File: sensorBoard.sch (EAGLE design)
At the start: 37 parts, among them U1 BME280, U2 nRF8001, U3 MIC5225-3.3v, U4 74HC4050D, Y1 16MHz, Y2 FC-255 32.7680K-A3

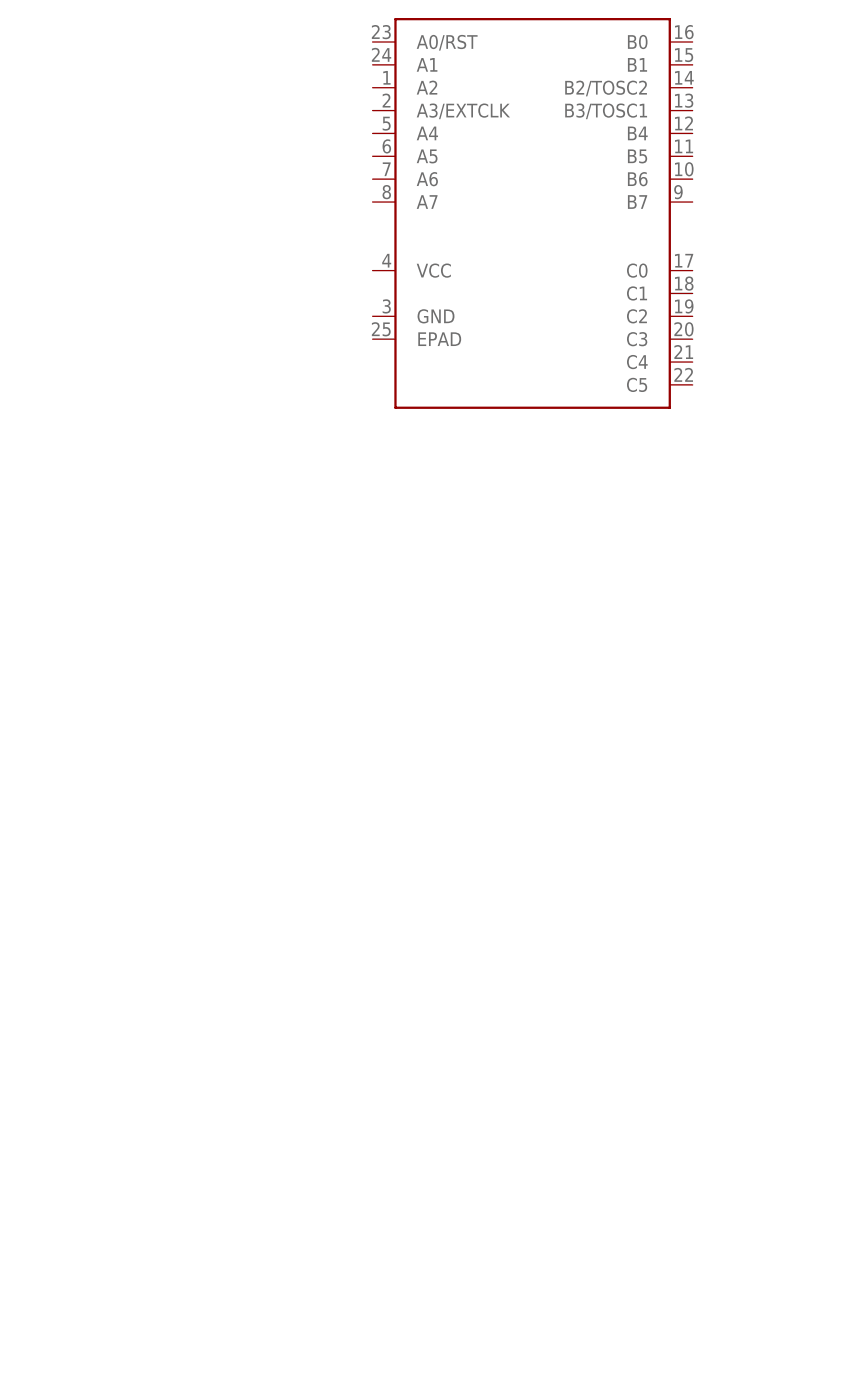
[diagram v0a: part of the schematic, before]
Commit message: Created proto PCB
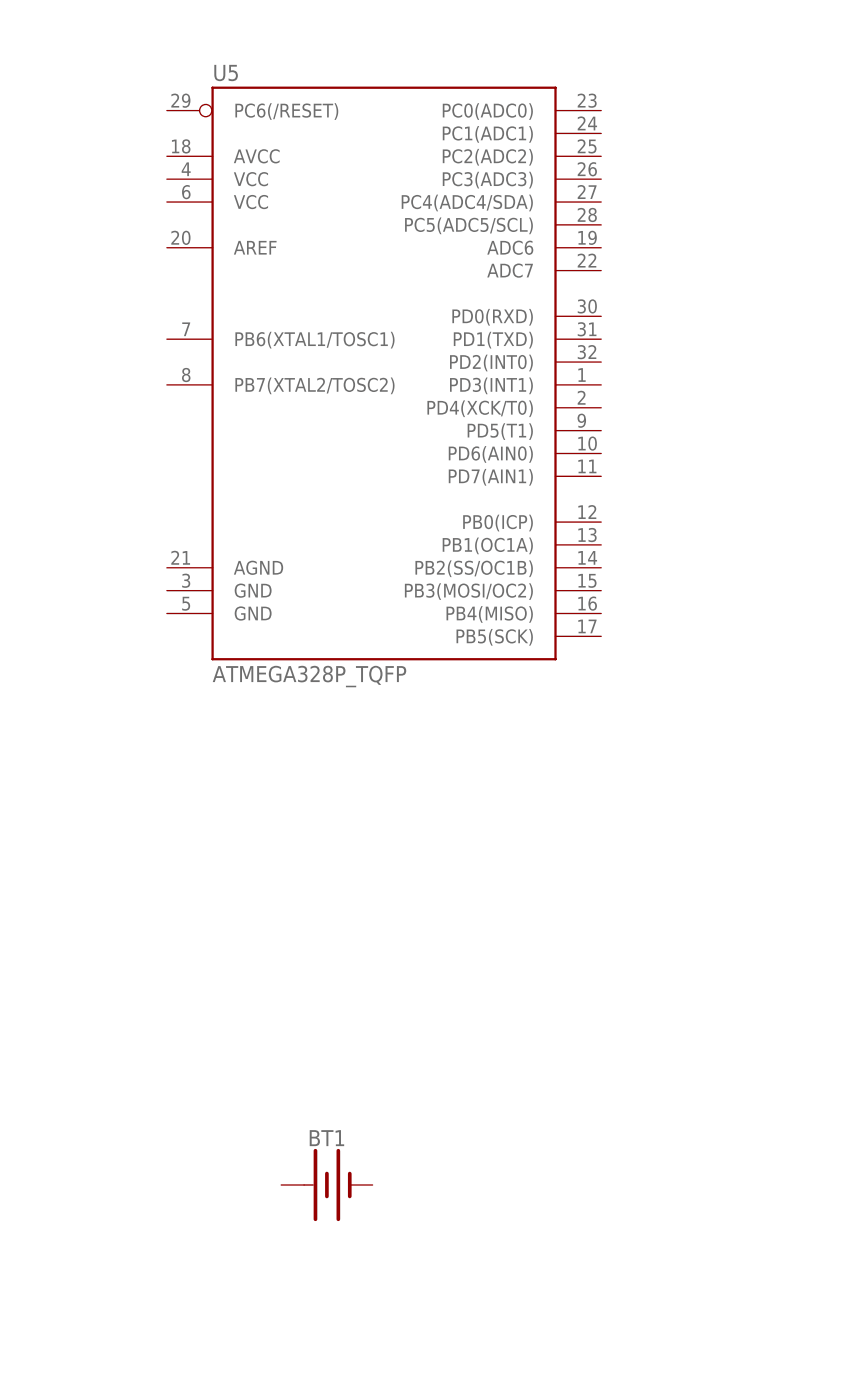
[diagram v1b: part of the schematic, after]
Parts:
- removed U$1: ATTINY3217, myLib:ATTINY3217
- added BT1: (no value), SparkFun-Batteries:BATTERY-20MM_PTH
- added U5: ATMEGA328P_TQFP, SparkFun-IC-Microcontroller:ATMEGA328P_TQFP
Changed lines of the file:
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@@
 <?xml version="1.0" encoding="utf-8"?>
 <!DOCTYPE eagle SYSTEM "eagle.dtd">
-<eagle version="9.3.0">
+<eagle version="9.2.2">
 <drawing>
 <settings>
@@
 <layer number="56" name="wert" color="7" fill="1" visible="no" active="no"/>
 <layer number="57" name="tCAD" color="7" fill="1" visible="no" active="no"/>
+<layer number="59" name="tCarbon" color="7" fill="1" visible="no" active="no"/>
+<layer number="60" name="bCarbon" color="7" fill="1" visible="no" active="no"/>
 <layer number="88" name="SimResults" color="9" fill="1" visible="yes" active="yes"/>
 <layer number="89" name="SimProbes" color="9" fill="1" visible="yes" active="yes"/>
@@
 <layer number="97" name="Info" color="7" fill="1" visible="yes" active="yes"/>
 <layer number="98" name="Guide" color="6" fill="1" visible="yes" active="yes"/>
+<layer number="99" name="SpiceOrder" color="7" fill="1" visible="yes" active="yes"/>
 <layer number="100" name="Muster" color="7" fill="1" visible="yes" active="yes"/>
 <layer number="101" name="Patch_Top" color="12" fill="4" visible="yes" active="yes"/>
@@
 <layer number="111" name="MPL" color="7" fill="1" visible="yes" active="yes"/>
 <layer number="112" name="tSilk" color="7" fill="1" visible="yes" active="yes"/>
+<layer number="113" name="IDFDebug" color="7" fill="1" visible="yes" active="yes"/>
+<layer number="114" name="Badge_Outline" color="7" fill="1" visible="yes" active="yes"/>
+<layer number="115" name="ReferenceISLANDS" color="7" fill="1" visible="yes" active="yes"/>
 <layer number="116" name="Patch_BOT" color="9" fill="4" visible="yes" active="yes"/>
+<layer number="118" name="Rect_Pads" color="7" fill="1" visible="yes" active="yes"/>
 <layer number="121" name="sName" color="7" fill="1" visible="yes" active="yes"/>
 <layer number="122" name="_bPlace" color="7" fill="1" visible="yes" active="yes"/>
@@
 <layer number="127" name="_tValues" color="7" fill="1" visible="yes" active="yes"/>
 <layer number="128" name="_bValues" color="7" fill="1" visible="yes" active="yes"/>
+<layer number="129" name="Mask" color="7" fill="1" visible="yes" active="yes"/>
 <layer number="131" name="tAdjust" color="7" fill="1" visible="no" active="yes"/>
 <layer number="132" name="bAdjust" color="7" fill="1" visible="no" active="yes"/>
@@
 <layer number="223" name="223bmp" color="24" fill="1" visible="no" active="no"/>
 <layer number="224" name="224bmp" color="25" fill="1" visible="no" active="no"/>
+<layer number="225" name="225bmp" color="7" fill="1" visible="yes" active="yes"/>
+<layer number="226" name="226bmp" color="7" fill="1" visible="yes" active="yes"/>
+<layer number="227" name="227bmp" color="7" fill="1" visible="yes" active="yes"/>
+<layer number="228" name="228bmp" color="7" fill="1" visible="yes" active="yes"/>
+<layer number="229" name="229bmp" color="7" fill="1" visible="yes" active="yes"/>
+<layer number="230" name="230bmp" color="7" fill="1" visible="yes" active="yes"/>
+<layer number="231" name="231bmp" color="7" fill="1" visible="yes" active="yes"/>
+<layer number="232" name="Eagle3D_PG2" color="7" fill="1" visible="yes" active="yes"/>
+<layer number="233" name="Eagle3D_PG3" color="7" fill="1" visible="yes" active="yes"/>
 <layer number="248" name="Housing" color="7" fill="1" visible="yes" active="yes"/>
 <layer number="249" name="Edge" color="7" fill="1" visible="yes" active="yes"/>
@@
 <layer number="251" name="SMDround" color="7" fill="1" visible="yes" active="yes"/>
 <layer number="254" name="cooling" color="7" fill="1" visible="yes" active="yes"/>
+<layer number="255" name="routoute" color="7" fill="1" visible="yes" active="yes"/>
 </layers>
 <schematic xreflabel="%F%N/%S.%C%R" xrefpart="/%S.%C%R">
@@
 <part name="FID3" library="microbuilder" deviceset="FIDUCIAL" device="&quot;&quot;"/>
 <part name="JP1" library="microbuilder" deviceset="HEADER-1X10" device="70MIL"/>
-<part name="U$1" library="myLib" library_urn="urn:adsk.eagle:library:9734266" deviceset="ATTINY3217" device="" package3d_urn="urn:adsk.eagle:package:9734100/1"/>
 <part name="U1" library="BME280" deviceset="BME280" device=""/>
+<part name="U5" library="SparkFun-IC-Microcontroller" library_urn="urn:adsk.eagle:library:525" deviceset="ATMEGA328P_TQFP" device="" package3d_urn="urn:adsk.eagle:package:38945/1" value="ATMEGA328P_TQFP"/>
+<part name="BT1" library="SparkFun-Batteries" library_urn="urn:adsk.eagle:library:508" deviceset="BATTERY" device="-20MM_PTH" package3d_urn="urn:adsk.eagle:package:37214/1"/>
 </parts>
 <sheets>
@@
 <attribute name="VALUE" x="72.39" y="17.78" size="1.778" layer="96"/>
 </instance>
-<instance part="U$1" gate="G$1" x="335.28" y="190.5" smashed="yes"/>
 <instance part="U1" gate="G$1" x="236.22" y="195.58" smashed="yes">
 <attribute name="NAME" x="226.0538" y="208.9231" size="1.786590625" layer="95"/>
 <attribute name="VALUE" x="226.0517" y="180.3276" size="1.782940625" layer="96"/>
 </instance>
+<instance part="U5" gate="U$1" x="320.04" y="172.72" smashed="yes">
+<attribute name="NAME" x="299.72" y="206.502" size="1.778" layer="95"/>
+<attribute name="VALUE" x="299.72" y="139.7" size="1.778" layer="96"/>
+</instance>
+<instance part="BT1" gate="G$1" x="312.42" y="83.82" smashed="yes">
+<attribute name="NAME" x="312.42" y="88.138" size="1.778" layer="95" font="vector" align="bottom-center"/>
+<attribute name="VALUE" x="312.42" y="79.502" size="1.778" layer="96" font="vector" align="top-center"/>
+</instance>
 </instances>
